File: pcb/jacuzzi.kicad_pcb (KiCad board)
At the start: 2 copper layers, 130 x 100 mm, 94 parts, among them J1 Conn_01x03, J10 Conn_01x02, J11 Conn_01x03, J12 Conn_01x03, J13 LOGO, J14 LOGO, J15 LOGO, J16 LOGO, J19 Conn_01x03, J2 Conn_01x03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

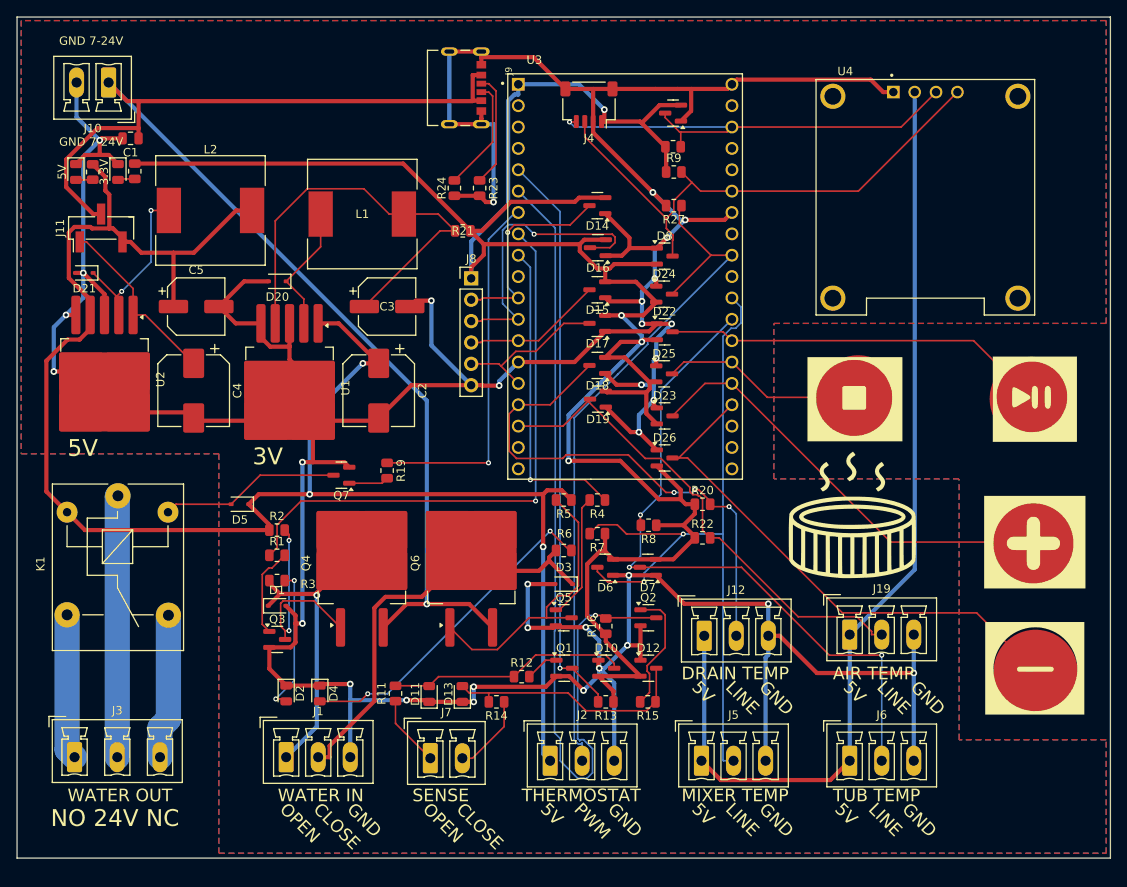
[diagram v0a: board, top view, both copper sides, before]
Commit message: added k2 and chagend the output fet ready for rewive
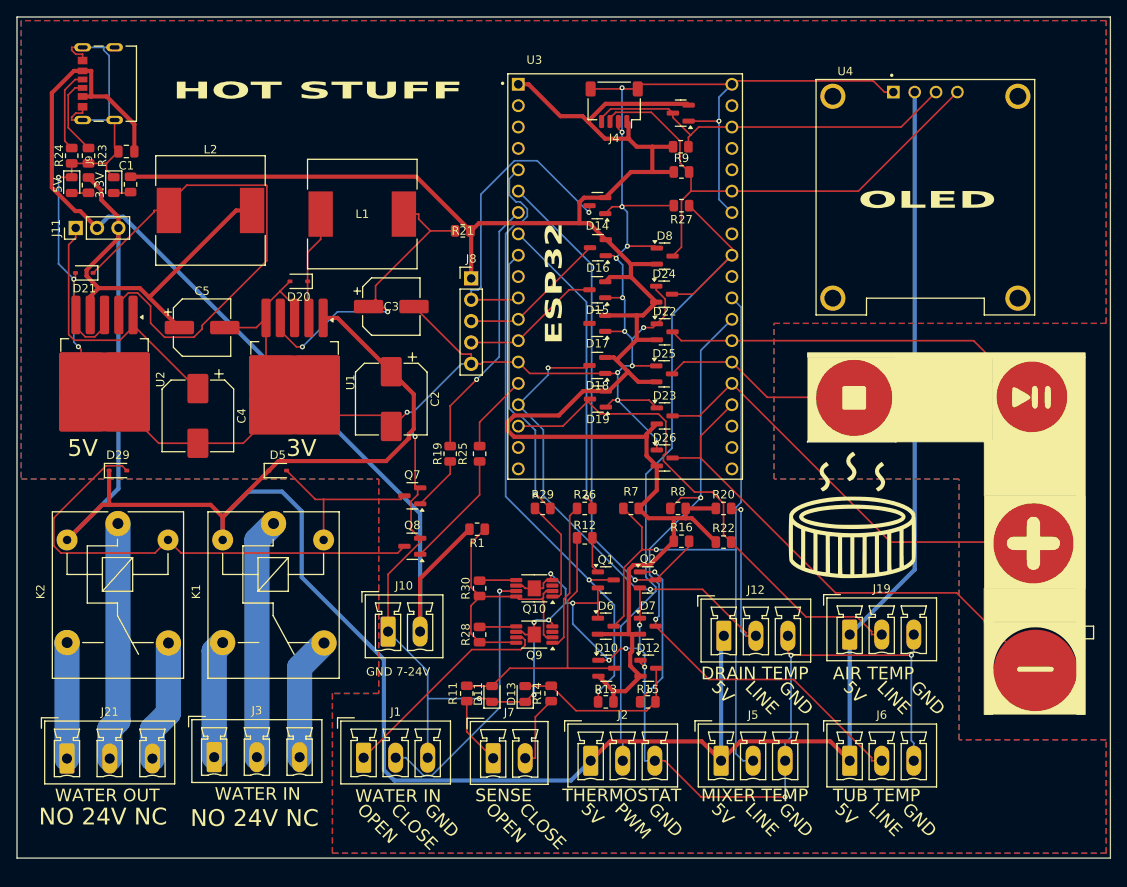
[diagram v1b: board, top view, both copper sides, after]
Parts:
- removed D1, D3: 1N5819WS, Diode_SMD:D_SOD-323
- removed D2, D4: GREEN LED, LED_SMD:LED_0805_2012Metric
- removed Q3, Q5: MMBT3904, Package_TO_SOT_SMD:SOT-23
- removed Q4, Q6: IRF4905STRLPBF, Package_TO_SOT_SMD:TO-263-2
- removed R2, R5: 3K3, Resistor_SMD:R_0805_2012Metric
- removed R3, R6: 2K2, Resistor_SMD:R_0805_2012Metric
- removed R4: 1K, Resistor_SMD:R_0805_2012Metric
- added D29: 1N5819, Diode_SMD:D_SOD-323, F.Cu at (86.0, 96.5)
- added J21: Conn_01x03, Connector_Phoenix_MC_HighVoltage:PhoenixContact_MCV_1,5_3-G-5.08_1x03_P5.08mm_Vertical, F.Cu at (79.9, 130.7)
- added K2: SRD-05VDC, Relay_THT:Relay_SPDT_SANYOU_SRD_Series_Form_C, F.Cu at (86.0, 102.8)
- added Q10: ~, Package_SO:HVSSOP-8-1EP_3x3mm_P0.65mm_EP1.57x1.89mm, F.Cu at (135.5, 110.5)
- added Q8: MMBT3904, Package_TO_SOT_SMD:SOT-23, F.Cu at (121.0, 105.5)
- added Q9: ~, Package_SO:HVSSOP-8-1EP_3x3mm_P0.65mm_EP1.57x1.89mm, F.Cu at (135.5, 116.0)
- added R25: 1K, Resistor_SMD:R_0805_2012Metric, F.Cu at (129.0, 94.5)
- added R26: 4k7, Resistor_SMD:R_0805_2012Metric, F.Cu at (141.5, 101.0)
- added R28: 100k, Resistor_SMD:R_0805_2012Metric, F.Cu at (129.0, 116.0)
- added R29: 4k7, Resistor_SMD:R_0805_2012Metric, F.Cu at (136.5, 101.0)
- added R30: 100k, Resistor_SMD:R_0805_2012Metric, F.Cu at (129.0, 110.5)
- J11: footprint Connector_PinHeader_2.54mm:PinHeader_1x03_P2.54mm_Vertical_SMD_Pin1Left -> Connector_PinHeader_2.54mm:PinHeader_1x03_P2.54mm_Vertical
- J8: footprint Connector_PinHeader_2.54mm:PinHeader_1x06_P2.54mm_Vertical -> Connector_PinHeader_2.54mm:PinHeader_1x05_P2.54mm_Vertical
- R1: value 1K -> 0R
- moved J10 73.3 mm to (118.1, 115.6), turned to 0 degrees
- moved J9 47.4 mm to (81.8, 50.5), turned to 90 degrees
- moved R23 46.7 mm to (82.5, 59.1)
- moved R24 45.7 mm to (80.5, 59.1)
- moved R1 24.0 mm to (128.7, 103.5), turned to 180 degrees
- moved K1 18.8 mm to (104.5, 102.8)
- moved R12 18.1 mm to (141.5, 104.5)
- moved J3 16.6 mm to (97.4, 130.6)
- moved R16 13.5 mm to (153.0, 104.9), turned to 0 degrees
- moved Q1 11.6 mm to (144.0, 109.5)
- moved J1 9.21 mm to (115.2, 130.6)
- moved Q7 8.79 mm to (121.0, 99.5)
- moved R11 8.47 mm to (127.5, 123.0)
- moved R19 7.76 mm to (125.5, 94.5)
- moved D13 7.47 mm to (134.4, 123.1)
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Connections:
- J10 pad 1: VS -> GND
- J10 pad 2: GND -> VS
- J8 pad 5: /GPIO_ADC4 -> GND
- R1 pad 1: /GPIO_BallValveOpen -> VS 5mills
- R1 pad 2: Net-(Q3-B) -> VS
- U3 pad 15: /GPIO_ADC4 -> /GPIO_solenoid
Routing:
- net GND: track 602.1 -> 539.9 mm, vias 33 -> 31
- net Net-(D29-A): track 0.00 -> 58.5 mm
- net VS: track 165.7 -> 120.4 mm, vias 1 -> 0
- net +5V: track 326.1 -> 369.3 mm, vias 3 -> 0
- net /GPIO_BallValveClose_Feedback: track 103.5 -> 60.7 mm
- net Net-(D21-K): track 20.3 -> 61.8 mm, vias 2 -> 0
- net Net-(D4-A): track 39.3 -> 0.00 mm, vias 2 -> 0
- net VS 5mills: track 0.00 -> 34.7 mm
- net Net-(Q5-C): track 34.5 -> 0.00 mm
- net /GPIO_BallValveOpen: track 68.5 -> 36.3 mm
- net /BallValveClose: track 61.7 -> 32.4 mm, vias 0 -> 1
- net /Solenoid_V: track 0.00 -> 28.3 mm
- net +3.3V: track 284.0 -> 257.4 mm, vias 4 -> 0
- net Net-(Q3-C): track 25.7 -> 0.00 mm, vias 2 -> 0
- net /BallValveOpen: track 50.5 -> 26.5 mm, vias 1 -> 0
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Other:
- board text added: "Conn_01x03"
- board text added: "ESP32"
- board text added: "HOT STUFF"
- board text added: "OLED"

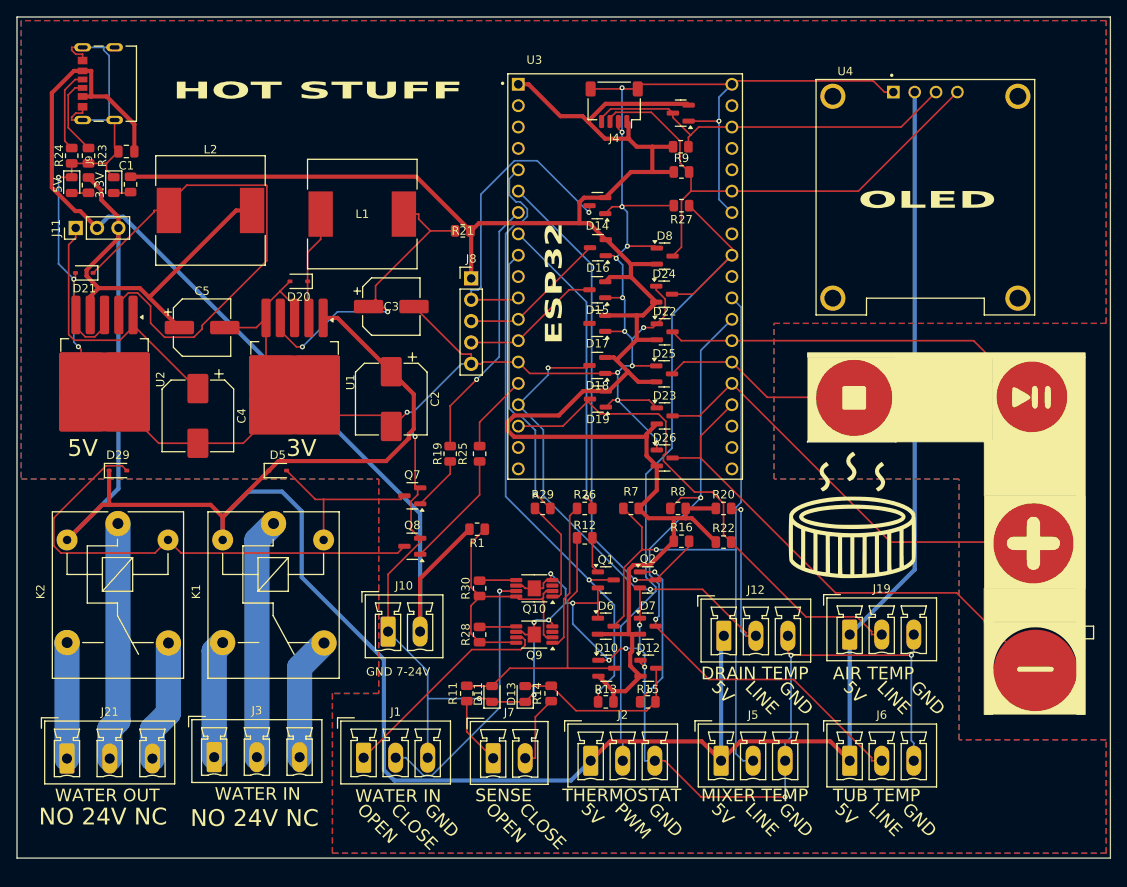
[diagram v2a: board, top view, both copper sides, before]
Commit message: move q9 and q10 and set 0.3mm track width for ball valve open and close and move the solenoid connector apart
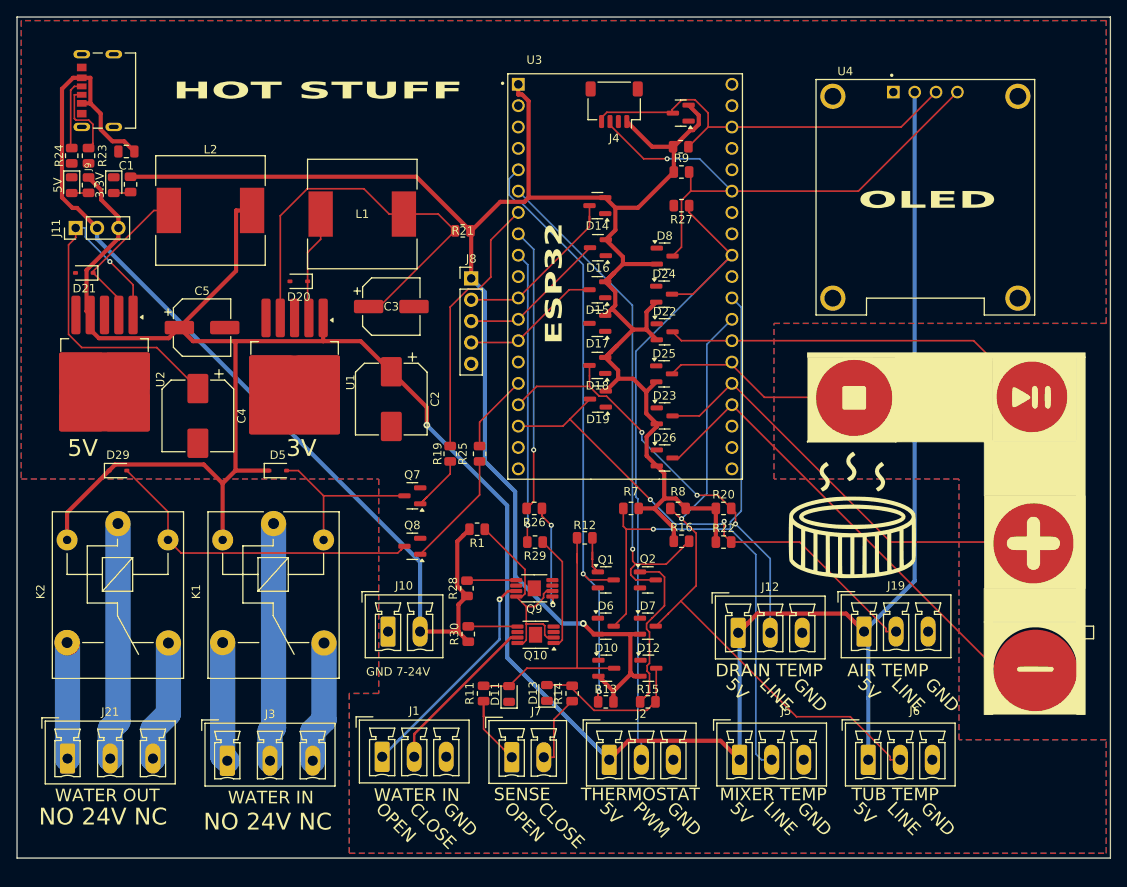
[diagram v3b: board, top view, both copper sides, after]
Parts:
- moved R26 6.00 mm to (135.5, 101.0), turned to 180 degrees
- moved R28 5.70 mm to (127.5, 110.5)
- moved R30 5.60 mm to (127.7, 115.9)
- moved Q10 5.53 mm to (135.7, 116.0)
- moved Q9 5.50 mm to (135.5, 110.5)
- moved R29 4.10 mm to (135.6, 105.0), turned to 180 degrees
- moved D13 2.58 mm to (137.0, 122.9)
- moved R14 2.50 mm to (140.0, 123.0)
- moved J1 2.21 mm to (117.4, 130.5)
- moved J6 2.21 mm to (175.2, 130.9)
- moved J2 2.21 mm to (144.4, 130.9)
- moved J5 2.21 mm to (159.9, 130.9)
- moved J7 2.21 mm to (132.8, 130.6)
- moved D11 2.03 mm to (132.5, 123.1)
- moved R11 2.00 mm to (129.5, 123.0)
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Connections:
- R28 pad 1: VS 5mills -> VS
- R30 pad 1: VS 5mills -> VS
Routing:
- net GND: track 539.9 -> 0.00 mm, vias 31 -> 0
- net +5V: track 369.3 -> 324.9 mm, vias 0 -> 1
- net Net-(D21-K): track 61.8 -> 18.5 mm
- net /GPIO9: track 73.0 -> 52.4 mm
- net Net-(D29-A): track 58.5 -> 40.2 mm
- net /GPIO_ADC1: track 37.0 -> 20.8 mm, vias 1 -> 0
- net /BallValveClose: track 32.4 -> 19.7 mm, vias 1 -> 0
- net Net-(U1-FB): track 38.2 -> 50.4 mm, vias 2 -> 0
- net Net-(J11-Pin_1): track 33.8 -> 44.9 mm, vias 0 -> 1
- net VS 5mills: track 34.7 -> 26.4 mm
- net Net-(Q9-IN): track 17.6 -> 13.2 mm, vias 0 -> 2
- net /GPIO_I2C_SDA: track 62.1 -> 65.7 mm, vias 0 -> 1
- net /GPIO_BallValveClose_Feedback: track 60.7 -> 63.6 mm
- net /GPIO_I2C_SCL: track 45.8 -> 48.8 mm
- net /BallValveOpen_Feedback: track 8.09 -> 11.0 mm
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
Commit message: moved the relay connector
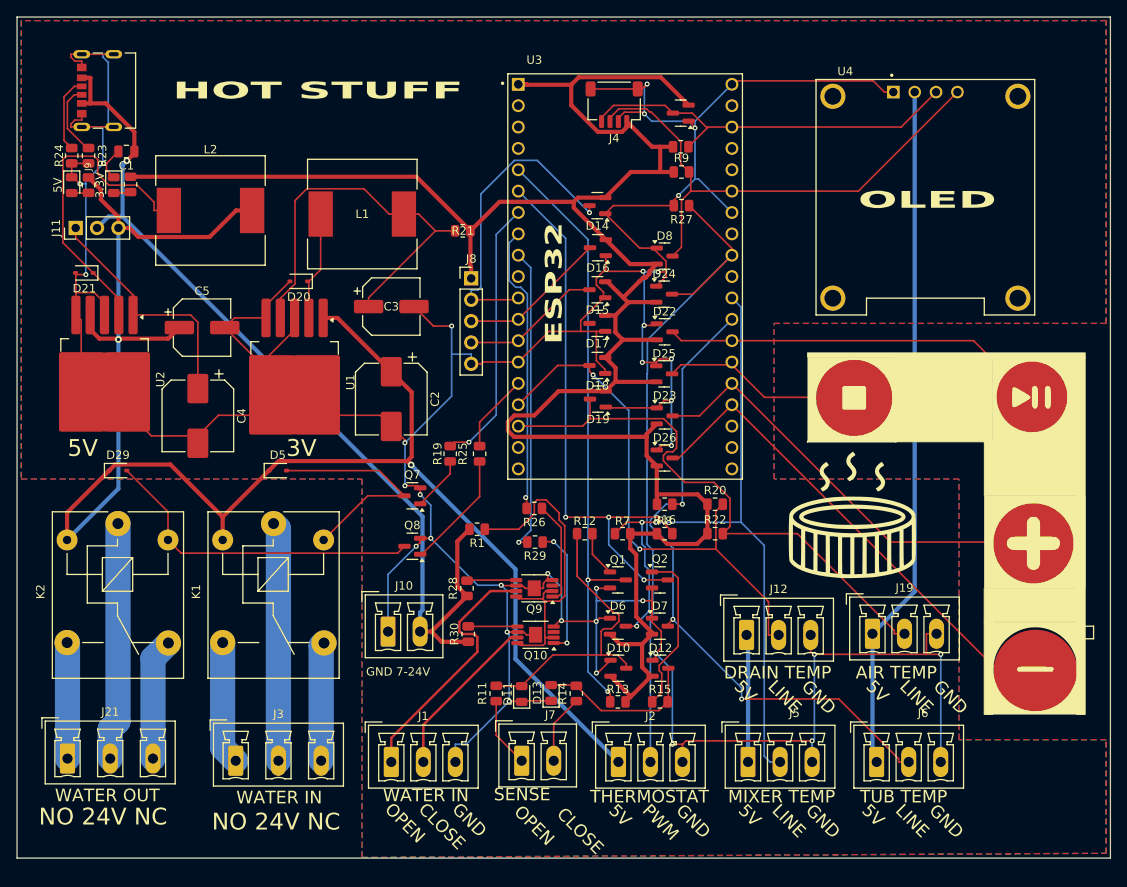
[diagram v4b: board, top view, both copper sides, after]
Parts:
- moved R7 3.16 mm to (146.0, 104.0)
- moved R16 2.19 mm to (151.0, 104.0)
- moved R8 1.66 mm to (151.0, 100.5), turned to 0 degrees
- moved D11 1.50 mm to (134.0, 123.1)
- moved R11 1.50 mm to (131.0, 123.0)
- moved D10 1.44 mm to (145.5, 120.0)
- moved D12 1.44 mm to (150.5, 120.0)
- moved D6 1.44 mm to (145.4, 115.0)
- moved D7 1.44 mm to (150.4, 115.0)
- moved Q1 1.44 mm to (145.4, 109.5)
- moved Q2 1.44 mm to (150.4, 109.5)
- moved R13 1.44 mm to (145.4, 124.0)
- moved R15 1.44 mm to (150.4, 124.0)
- moved R22 1.41 mm to (157.0, 104.0)
- moved J7 1.25 mm to (134.0, 131.0)
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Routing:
- net GND: track 0.00 -> 554.1 mm, vias 0 -> 34
- net +5V: track 324.9 -> 298.2 mm, vias 1 -> 2
- net Net-(D21-K): track 18.5 -> 38.3 mm
- net /GPIO_ADC1: track 20.8 -> 37.2 mm, vias 0 -> 1
- net Net-(J11-Pin_1): track 44.9 -> 29.1 mm, vias 1 -> 0
- net VS 5mills: track 26.4 -> 39.5 mm
- net /GPIO9: track 52.4 -> 63.4 mm, vias 3 -> 2
- net VS: track 119.1 -> 111.4 mm, vias 0 -> 1
- net /GPIO10: track 60.5 -> 67.8 mm, vias 2 -> 0
- net Net-(D5-A): track 20.5 -> 27.0 mm
- net /GPIO_I2C_SDA: track 65.7 -> 62.5 mm, vias 1 -> 0
- net Net-(D10-COM): track 32.9 -> 36.1 mm
- net /GPIO_BallValveClose_Feedback: track 63.6 -> 66.8 mm, vias 1 -> 3
- net /BallValveOpen: track 27.9 -> 30.9 mm, vias 1 -> 0
- net /BallValveOpen_Feedback: track 11.0 -> 8.34 mm
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
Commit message: fixed resistor label
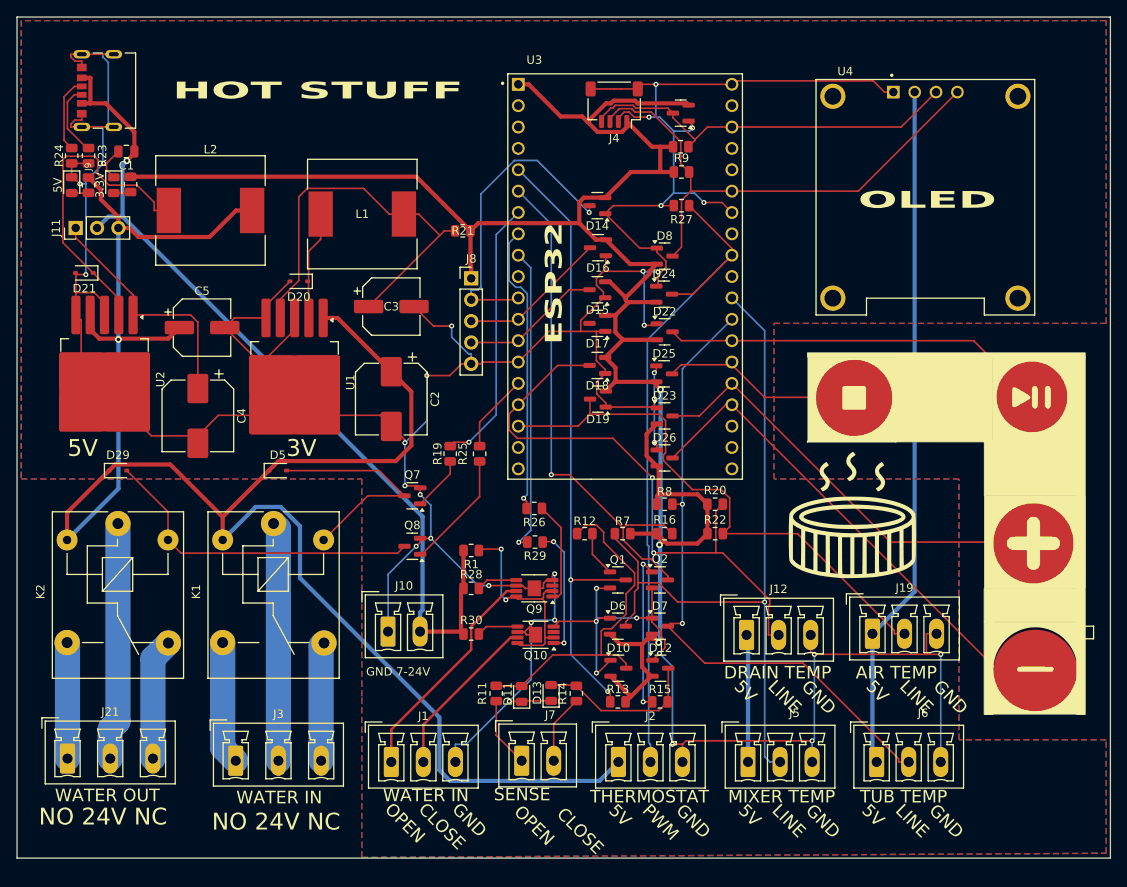
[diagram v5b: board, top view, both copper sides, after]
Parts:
- moved R1 2.62 mm to (128.0, 106.0)
- moved R28 0.50 mm to (128.0, 110.5), turned to 0 degrees
- moved R30 0.35 mm to (128.0, 115.9), turned to 0 degrees
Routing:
- net +5V: track 298.2 -> 321.5 mm, vias 2 -> 1
- net +3.3V: track 261.3 -> 246.0 mm, vias 0 -> 3
- net VS 5mills: track 39.5 -> 25.4 mm, vias 0 -> 2
- net /GPIO9: track 63.4 -> 69.9 mm
- net VS: track 111.4 -> 105.3 mm
- net /GPIO_BallValveClose_Feedback: track 66.8 -> 61.9 mm, vias 3 -> 1
- net Net-(D10-COM): track 36.1 -> 40.2 mm
- net /BallValveOpen: track 30.9 -> 27.1 mm
- net /GPIO_Dallas2: track 80.2 -> 77.2 mm, vias 3 -> 2
- net GND: track 554.1 -> 551.1 mm, vias 34 -> 35
- net /GPIO_BallValveOpen_Feedback: track 72.3 -> 74.3 mm
- net /GPIO10: track 67.8 -> 66.1 mm
- net /GPIO_Dallas1: track 88.4 -> 87.0 mm, vias 3 -> 1
- net Net-(Q9-DELAY): track 5.88 -> 4.84 mm
- net Net-(Q10-DELAY): track 5.86 -> 4.96 mm
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
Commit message: minor fixes and ordered
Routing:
- net +3.3V: track 246.0 -> 273.1 mm, vias 3 -> 0
- net +5V: track 321.5 -> 344.6 mm, vias 1 -> 3
- net /GPIO_I2C_SDA: track 62.5 -> 81.5 mm, vias 0 -> 1
- net /GPIO_Dallas2: track 77.2 -> 94.6 mm
- net /GPIO_ADC1: track 37.1 -> 23.6 mm
- net Net-(D21-K): track 38.3 -> 26.6 mm
- net VS: track 105.3 -> 115.2 mm
- net /GPIO_ADC2: track 17.7 -> 25.4 mm, vias 0 -> 1
- net Net-(D5-A): track 27.0 -> 20.7 mm
- net /GPIO_I2C_SCL: track 46.4 -> 51.7 mm
- net GND: track 551.1 -> 556.0 mm, vias 35 -> 31
- net VS 5mills: track 25.4 -> 29.9 mm, vias 2 -> 3
- net Net-(D10-COM): track 40.2 -> 35.8 mm
- net Net-(J11-Pin_1): track 29.1 -> 25.1 mm
- net /GPIO_BallValveOpen_Feedback: track 74.3 -> 70.8 mm
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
